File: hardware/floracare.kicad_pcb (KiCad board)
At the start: 2 copper layers, 100 x 100 mm, 25 parts, among them J1 USB_C_Receptacle_USB2.0_16P, J2 Conn_01x04_Socket, J4 Conn_01x04_Socket, J5 Conn_01x14_Socket, J6 Conn_01x05_Socket, SW1 SW_Push, SW2 SW_Push, U1 AMS1117-3.3, U2 ESP32-S3-WROOM-1

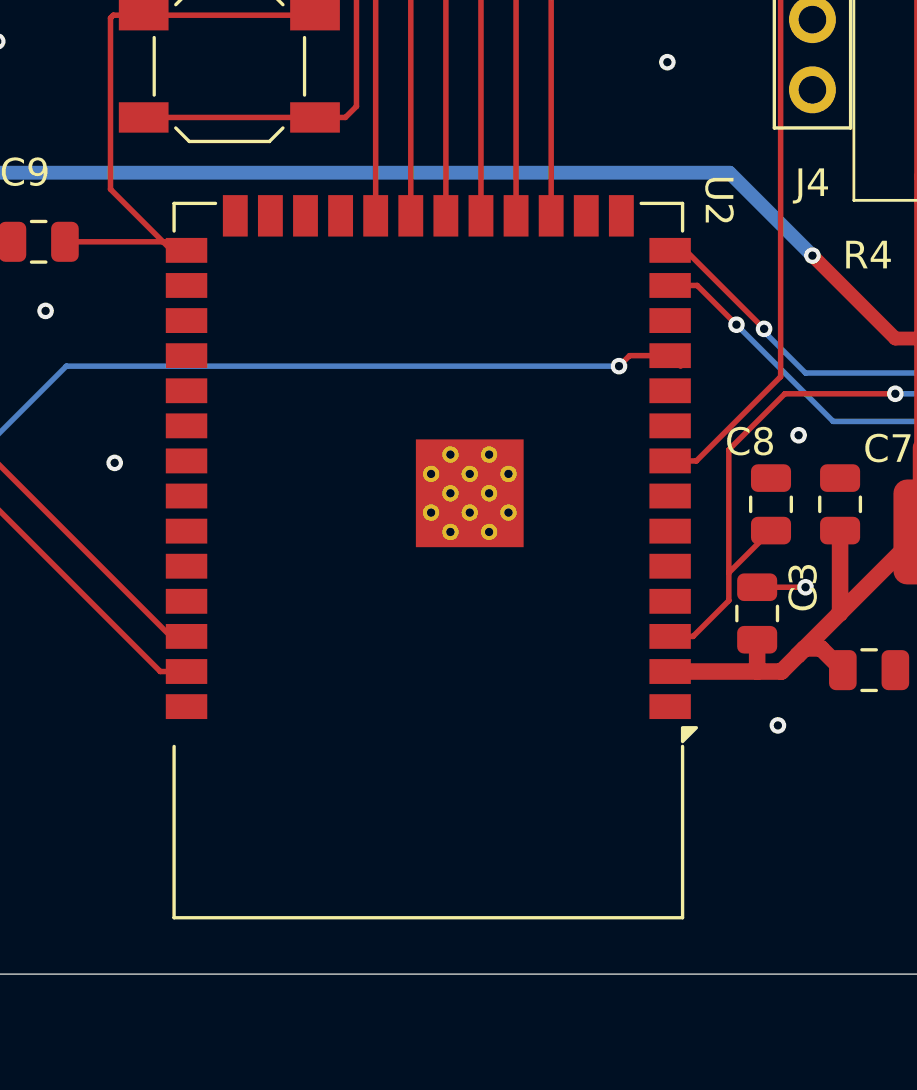
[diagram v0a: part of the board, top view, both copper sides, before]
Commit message: Fixing ESP32 -S3 WRROM1 MODULE Warning [DRC 100% STABLE]
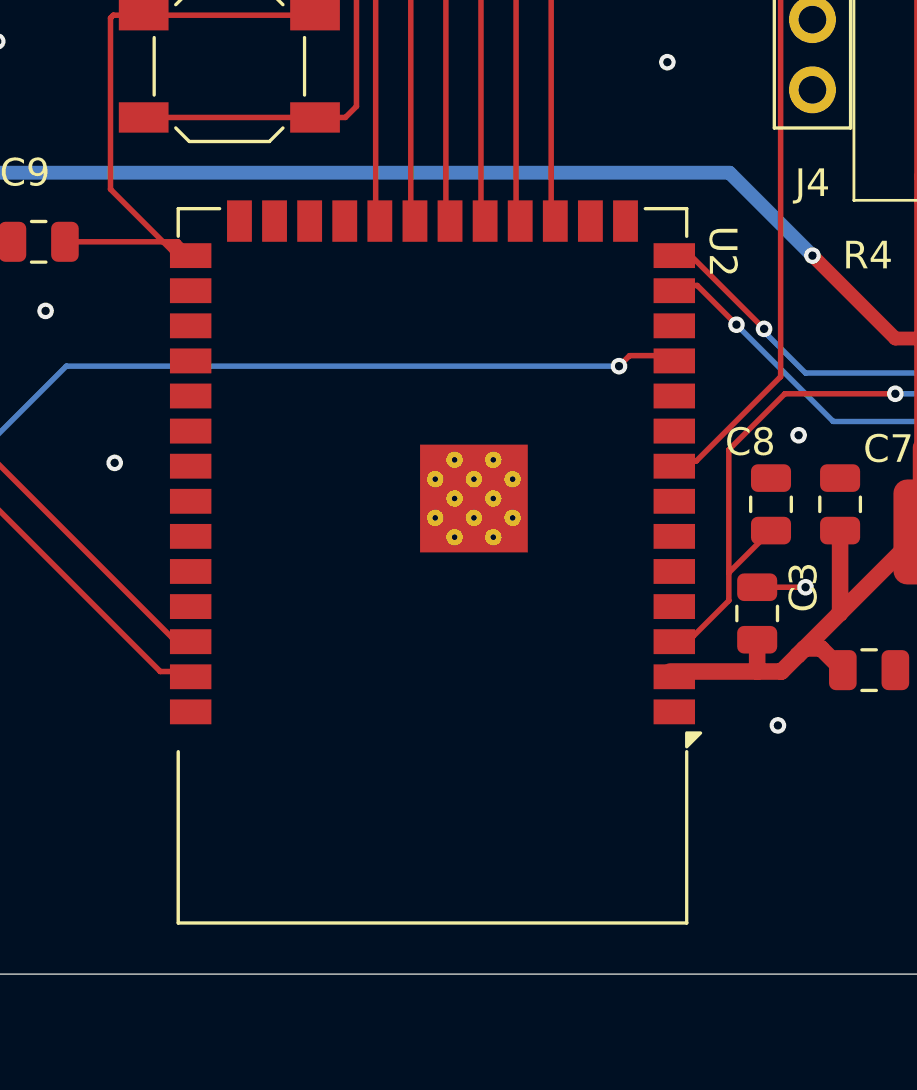
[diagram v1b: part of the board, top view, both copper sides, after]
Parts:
- moved U2 0.24 mm to (192.7, 111.1)
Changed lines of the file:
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@@
 	(footprint "RF_Module:ESP32-S3-WROOM-1"
 		(layer "F.Cu")
-		(at 192.52 110.91 180)
+		(at 192.67 111.1 180)
 		(descr "2.4 GHz Wi-Fi and Bluetooth module  https://www.espressif.com/sites/default/files/documentation/esp32-s3-wroom-1_wroom-1u_datasheet_en.pdf")
 		(tags "2.4 GHz Wi-Fi and Bluetooth module")
 		(property "Reference" "U2"
-			(at -10.5 13.06 270)
+			(at -10.5 11.4 270)
 			(unlocked yes)
 			(layer "F.SilkS")
@@
 		)
 		(property "Value" "ESP32-S3-WROOM-1"
-			(at -0.17 -5.34 0)
+			(at 0 14.6 180)
 			(unlocked yes)
 			(layer "F.Fab")
@@
 			(at -2.9 1.76 270)
 			(size 0.6 0.6)
-			(drill 0.3)
+			(drill 0.2)
 			(property pad_prop_heatsink)
 			(layers "*.Cu" "F.Mask")
@@
 			(at -2.9 3.16 180)
 			(size 0.6 0.6)
-			(drill 0.3)
+			(drill 0.2)
 			(property pad_prop_heatsink)
 			(layers "*.Cu" "F.Mask")
@@
 			(at -2.2 1.06 180)
 			(size 0.6 0.6)
-			(drill 0.3)
+			(drill 0.2)
 			(property pad_prop_heatsink)
 			(layers "*.Cu" "F.Mask")
@@
 			(at -2.2 2.46 180)
 			(size 0.6 0.6)
-			(drill 0.3)
+			(drill 0.2)
 			(property pad_prop_heatsink)
 			(layers "*.Cu" "F.Mask")
@@
 			(at -2.2 3.86 180)
 			(size 0.6 0.6)
-			(drill 0.3)
+			(drill 0.2)
 			(property pad_prop_heatsink)
 			(layers "*.Cu" "F.Mask")
@@
 			(at -1.5 1.76 180)
 			(size 0.6 0.6)
-			(drill 0.3)
+			(drill 0.2)
 			(property pad_prop_heatsink)
 			(layers "*.Cu" "F.Mask")
@@
 			(at -1.5 3.16 180)
 			(size 0.6 0.6)
-			(drill 0.3)
+			(drill 0.2)
 			(property pad_prop_heatsink)
 			(layers "*.Cu" "F.Mask")
@@
 			(at -0.8 1.06 180)
 			(size 0.6 0.6)
-			(drill 0.3)
+			(drill 0.2)
 			(property pad_prop_heatsink)
 			(layers "*.Cu" "F.Mask")
@@
 			(at -0.8 2.46 180)
 			(size 0.6 0.6)
-			(drill 0.3)
+			(drill 0.2)
 			(property pad_prop_heatsink)
 			(layers "*.Cu" "F.Mask")
@@
 			(at -0.8 3.86 180)
 			(size 0.6 0.6)
-			(drill 0.3)
+			(drill 0.2)
 			(property pad_prop_heatsink)
 			(layers "*.Cu" "F.Mask")
@@
 			(at -0.1 1.76 180)
 			(size 0.6 0.6)
-			(drill 0.3)
+			(drill 0.2)
 			(property pad_prop_heatsink)
 			(layers "*.Cu" "F.Mask")
@@
 			(at -0.1 3.16 180)
 			(size 0.6 0.6)
-			(drill 0.3)
+			(drill 0.2)
 			(property pad_prop_heatsink)
 			(layers "*.Cu" "F.Mask")
@@
 			(polygon
 				(pts
-					(xy 216.52 117.66) (xy 168.52 117.66) (xy 168.52 138.66) (xy 216.52 138.66)
+					(xy 216.67 117.85) (xy 168.67 117.85) (xy 168.67 138.85) (xy 216.67 138.85)
 				)
 			)

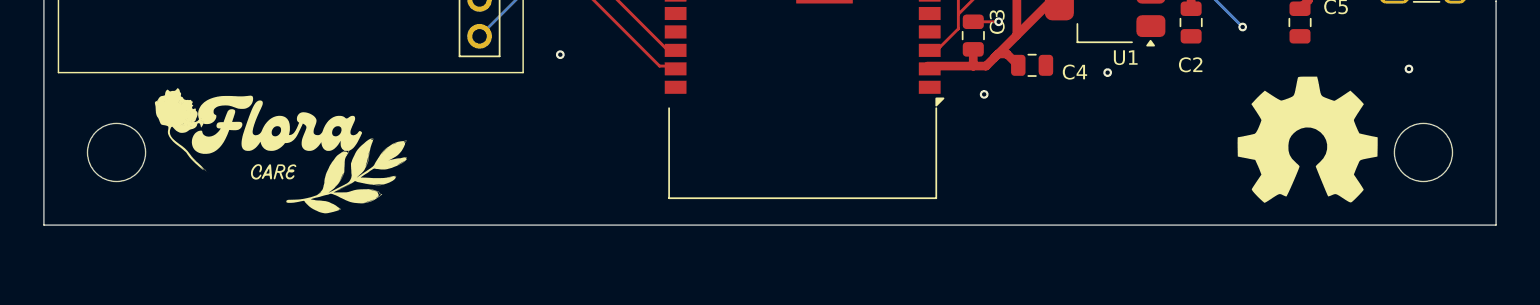
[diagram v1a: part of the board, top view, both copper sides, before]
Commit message: Adding mounting holes
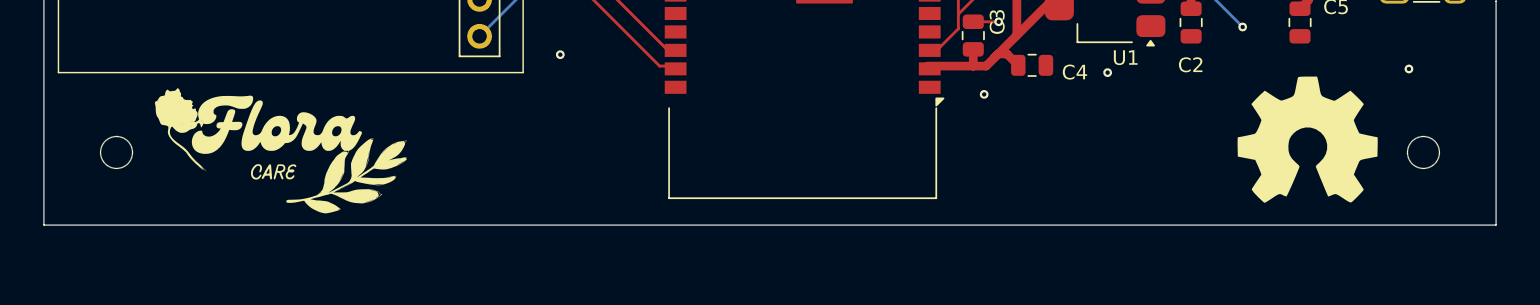
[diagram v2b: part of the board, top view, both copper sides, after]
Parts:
- added REF**: MountingHole_2.2mm_M2, MountingHole:MountingHole_2.2mm_M2, F.Cu at (235.4, 120.8)
- added REF**: MountingHole_2.2mm_M2, MountingHole:MountingHole_2.2mm_M2, F.Cu at (145.4, 120.8)
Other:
- outline, holes or cut-outs redrawn
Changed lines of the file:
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@@
 		)
 	)
+	(footprint "MountingHole:MountingHole_2.2mm_M2"
+		(layer "F.Cu")
+		(at 235.42 120.85)
+		(descr "Mounting Hole 2.2mm, M2, no annular, generated by kicad-footprint-generator mountinghole.py")
+		(tags "mountinghole M2")
+		(property "Reference" "REF**"
+			(at 0 -3.15 0)
+			(layer "F.SilkS")
+			(hide yes)
+			(effects
+				(font
+					(size 1 1)
+					(thickness 0.15)
+				)
+			)
+		)
+		(property "Value" "MountingHole_2.2mm_M2"
+			(at 0 3.15 0)
+			(layer "F.Fab")
+			(effects
+				(font
+					(size 1 1)
+					(thickness 0.15)
+				)
+			)
+		)
+		(property "Datasheet" ""
+			(at 0 0 0)
+			(layer "F.Fab")
+			(hide yes)
+			(effects
+				(font
+					(size 1.27 1.27)
+					(thickness 0.15)
+				)
+			)
+		)
+		(property "Description" ""
+			(at 0 0 0)
+			(layer "F.Fab")
+			(hide yes)
+			(effects
+				(font
+					(size 1.27 1.27)
+					(thickness 0.15)
+				)
+			)
+		)
+		(attr exclude_from_pos_files exclude_from_bom)
+		(fp_circle
+			(center 0 0)
+			(end 2.2 0)
+			(stroke
+				(width 0.15)
+				(type solid)
+			)
+			(fill no)
+			(layer "Cmts.User")
+		)
+		(fp_circle
+			(center 0 0)
+			(end 2.45 0)
+			(stroke
+				(width 0.05)
+				(type solid)
+			)
+			(fill no)
+			(layer "F.CrtYd")
+		)
+		(fp_text user "${REFERENCE}"
+			(at 0 0 0)
+			(layer "F.Fab")
+			(effects
+				(font
+					(size 1 1)
+					(thickness 0.15)
+				)
+			)
+		)
+		(pad "" np_thru_hole circle
+			(at 0 0)
+			(size 2.2 2.2)
+			(drill 2.2)
+			(layers "*.Cu" "*.Mask")
+		)
+		(embedded_fonts no)
+	)
 	(footprint "Capacitor_SMD:C_0805_2012Metric"
 		(layer "F.Cu")
@@
 		)
 	)
+	(footprint "MountingHole:MountingHole_2.2mm_M2"
+		(layer "F.Cu")
+		(at 145.42 120.85)
+		(descr "Mounting Hole 2.2mm, M2, no annular, generated by kicad-footprint-generator mountinghole.py")
+		(tags "mountinghole M2")
+		(property "Reference" "REF**"
+			(at 0 -3.15 0)
+			(layer "F.SilkS")
+			(hide yes)
+			(effects
+				(font
+					(size 1 1)
+					(thickness 0.15)
+				)
+			)
+		)
+		(property "Value" "MountingHole_2.2mm_M2"
+			(at 0 3.15 0)
+			(layer "F.Fab")
+			(effects
+				(font
+					(size 1 1)
+					(thickness 0.15)
+				)
+			)
+		)
+		(property "Datasheet" ""
+			(at 0 0 0)
+			(layer "F.Fab")
+			(hide yes)
+			(effects
+				(font
+					(size 1.27 1.27)
+					(thickness 0.15)
+				)
+			)
+		)
+		(property "Description" ""
+			(at 0 0 0)
+			(layer "F.Fab")
+			(hide yes)
+			(effects
+				(font
+					(size 1.27 1.27)
+					(thickness 0.15)
+				)
+			)
+		)
+		(attr exclude_from_pos_files exclude_from_bom)
+		(fp_circle
+			(center 0 0)
+			(end 2.2 0)
+			(stroke
+				(width 0.15)
+				(type solid)
+			)
+			(fill no)
+			(layer "Cmts.User")
+		)
+		(fp_circle
+			(center 0 0)
+			(end 2.45 0)
+			(stroke
+				(width 0.05)
+				(type solid)
+			)
+			(fill no)
+			(layer "F.CrtYd")
+		)
+		(fp_text user "${REFERENCE}"
+			(at 0 0 0)
+			(layer "F.Fab")
+			(effects
+				(font
+					(size 1 1)
+					(thickness 0.15)
+				)
+			)
+		)
+		(pad "" np_thru_hole circle
+			(at 0 0)
+			(size 2.2 2.2)
+			(drill 2.2)
+			(layers "*.Cu" "*.Mask")
+		)
+		(embedded_fonts no)
+	)
 	(footprint "Capacitor_SMD:C_0805_2012Metric"
 		(layer "F.Cu")
@@
 		(layer "F.SilkS")
 	)
-	(gr_circle
-		(center 145.42 120.85)
-		(end 147.42 120.85)
-		(stroke
-			(width 0.05)
-			(type default)
-		)
-		(fill no)
-		(layer "Edge.Cuts")
-	)
 	(gr_line
 		(start 140.42 125.85)
@@
 		(layer "Edge.Cuts")
 	)
-	(gr_circle
-		(center 235.42 120.85)
-		(end 237.42 120.85)
-		(stroke
-			(width 0.05)
-			(type default)
-		)
-		(fill no)
-		(layer "Edge.Cuts")
-	)
